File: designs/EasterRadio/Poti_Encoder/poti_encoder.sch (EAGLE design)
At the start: 12 parts

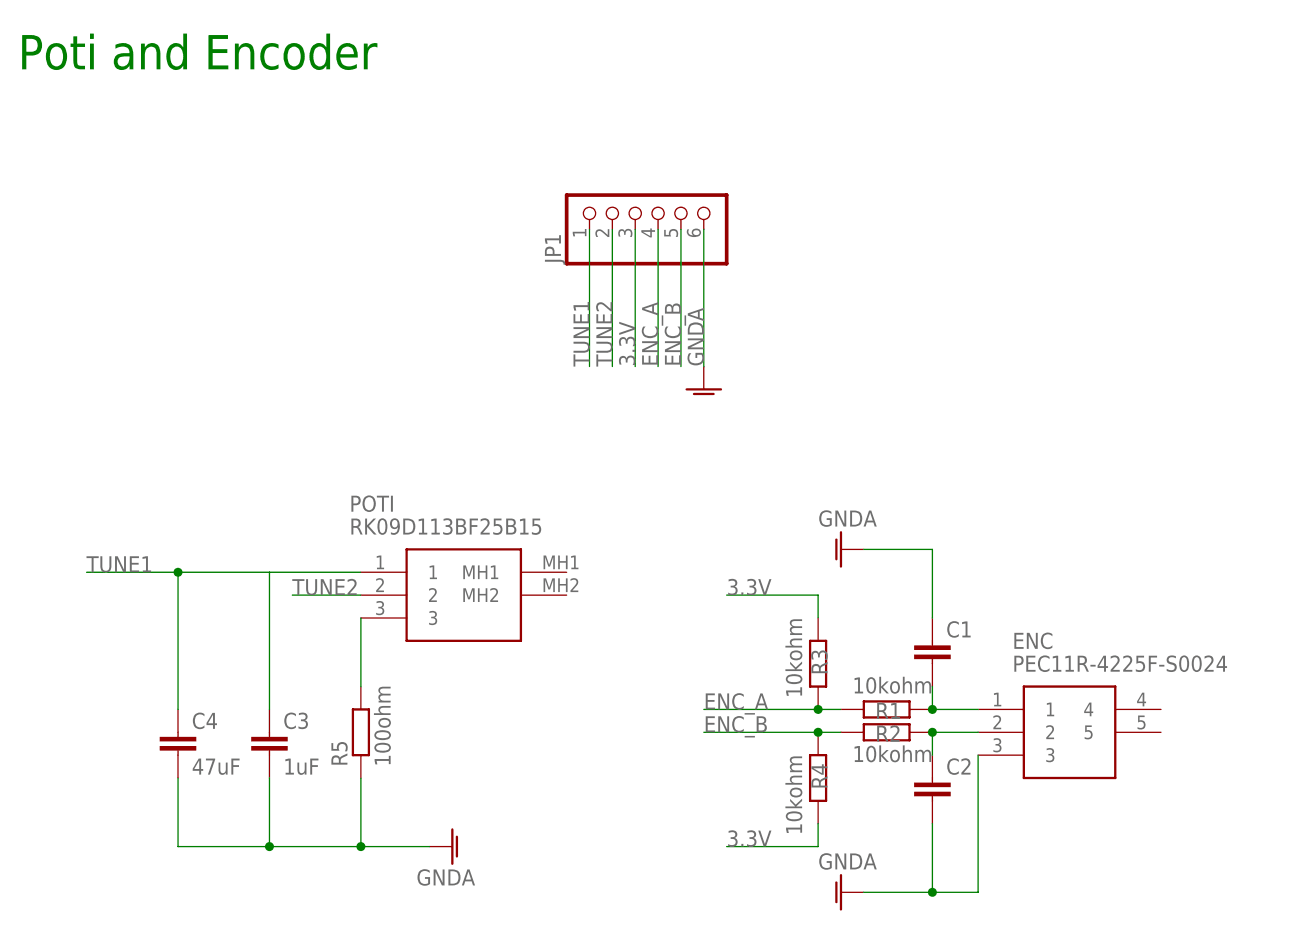
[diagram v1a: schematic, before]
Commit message: changed poti and encoder pcb to correct schematic and brd + mainboard change for push btn on rotary encoder
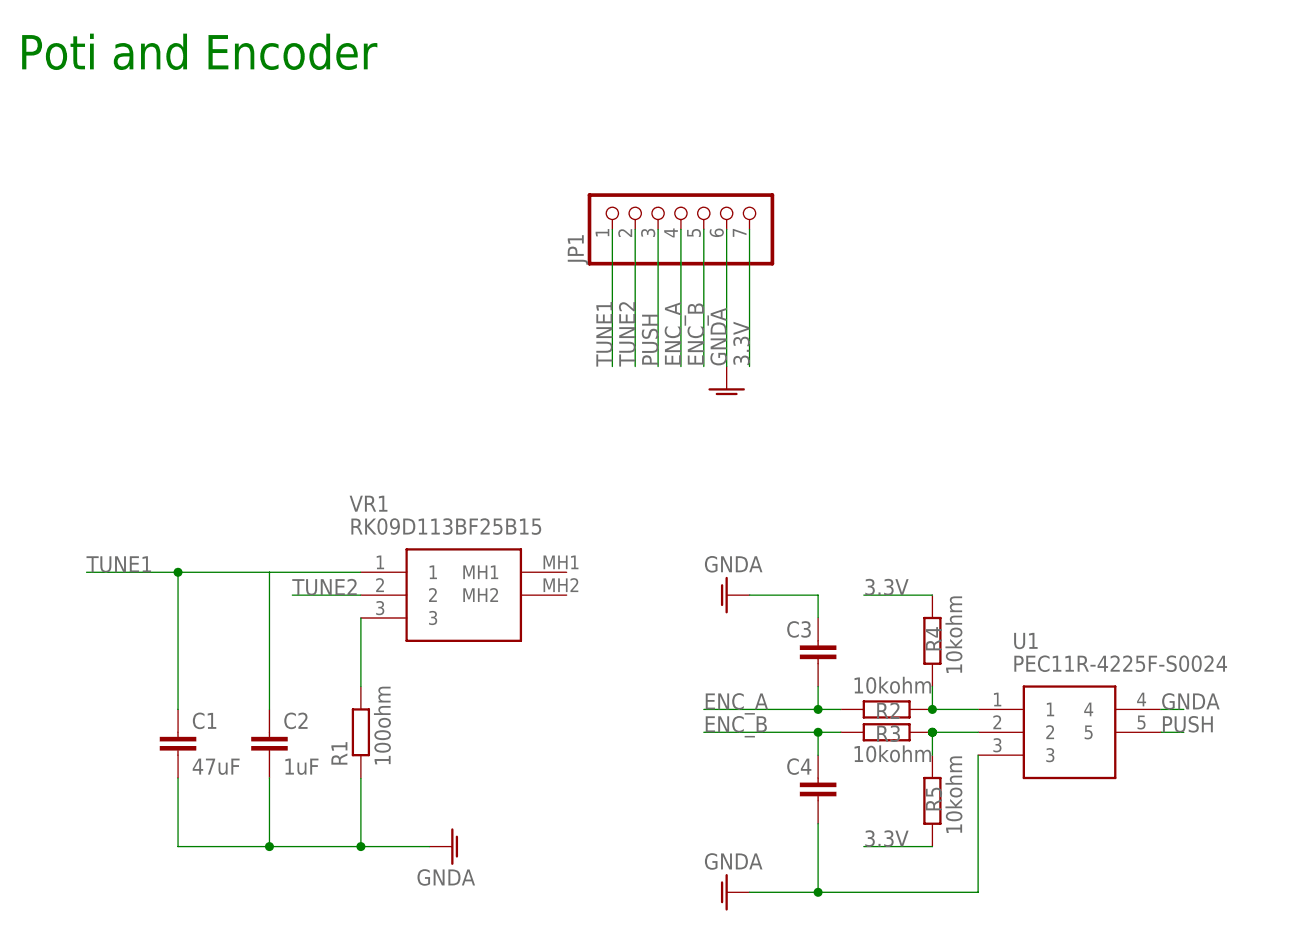
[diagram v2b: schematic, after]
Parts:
- C1: value (none) -> 47uF; device CommonParts:C-EU_805C0805 -> CommonParts:C-EU_1206C1206
- C2: value (none) -> 1uF
- C3: value 1uF -> (none)
- C4: value 47uF -> (none); device CommonParts:C-EU_1206C1206 -> CommonParts:C-EU_805C0805
- JP1: device pinhead:PINHD-1X6 -> pinhead:PINHD-1X7
- R1: value 10kohm -> 100ohm
- R5: value 100ohm -> 10kohm
- renumbered ENC to U1, POTI to VR1
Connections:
- new net PUSH: JP1.3, U1.5
- net 3.3V: now also JP1.7, R4.2, R5.1; no longer JP1.3, R3.2, R4.1
- net ENC_A: now also C3.2, R2.1; no longer R1.1, R3.1
- net ENC_B: now also C4.1, R3.1; no longer R2.1, R4.2
- net GNDA: now also C1.2, C3.1, R1.1, U1.4; no longer C1.1, C3.2, R5.1
- net N$1: now also R2.2, R4.1; no longer C1.2, R1.2
- net N$2: now also R3.2, R5.2; no longer C2.1, R2.2
- net N$4: now also R1.2; no longer R5.2
- net TUNE1: now also C1.1, C2.1; no longer C3.1, C4.1
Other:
- moved on the sheet: C1, C2, C3, C4, R1, R2, R3, R4, R5

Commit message: Fixed encoder issue: Terminal C connected to 3.3V instead of GND which is in contrast to the datasheet circuit diagram but is working.
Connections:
- net 3.3V: now also U1.3
- net GNDA: no longer U1.3
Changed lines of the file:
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@@
 <wire x1="101.6" y1="12.7" x2="93.98" y2="12.7" width="0.1524" layer="91" grouprefs="ENCODER"/>
 <label x="93.98" y="12.7" size="1.778" layer="95" grouprefs="ENCODER"/>
+<pinref part="U1" gate="G$1" pin="3"/>
+<wire x1="106.68" y1="22.86" x2="106.68" y2="12.7" width="0.1524" layer="91"/>
+<wire x1="106.68" y1="12.7" x2="101.6" y2="12.7" width="0.1524" layer="91"/>
+<junction x="101.6" y="12.7"/>
 </segment>
 <segment>
@@
 <wire x1="88.9" y1="7.62" x2="81.28" y2="7.62" width="0.1524" layer="91" grouprefs="ENCODER"/>
 <pinref part="GND1" gate="1" pin="GNDA"/>
-<pinref part="U1" gate="G$1" pin="3"/>
-<wire x1="106.68" y1="22.86" x2="106.68" y2="7.62" width="0.1524" layer="91" grouprefs="ENCODER"/>
-<wire x1="106.68" y1="7.62" x2="88.9" y2="7.62" width="0.1524" layer="91" grouprefs="ENCODER"/>
-<junction x="88.9" y="7.62" grouprefs="ENCODER"/>
 </segment>
 <segment>

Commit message: added final revisions to amplifier power radio ic and control pcbs
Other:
- note added: "Revision 1 02.04.21"
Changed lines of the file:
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@@
 <text x="0" y="99.06" size="3.81" layer="91">Poti and Encoder</text>
 <frame x1="0" y1="0" x2="144.78" y2="96.52" columns="8" rows="5" layer="91"/>
+<text x="43.18" y="99.06" size="1.778" layer="91">Revision 1 02.04.21</text>
 </plain>
 <instances>
